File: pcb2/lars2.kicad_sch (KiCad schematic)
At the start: 32 parts, among them SW1 RotaryEncoder_Switch, SW2 SW_Push, SW3 SW_Push, SW4 SW_Push, SW5 SW_Push, SW6 SW_Push, SW7 SW_Push, SW8 SW_Push, SW9 SW_Push, U1 Pico, U2 Charger, U3 MOSFET, U4 MOSFET, U5 MOSFET, U6 STEP_UP, U7 STEP_UP, U8 STEP_UP

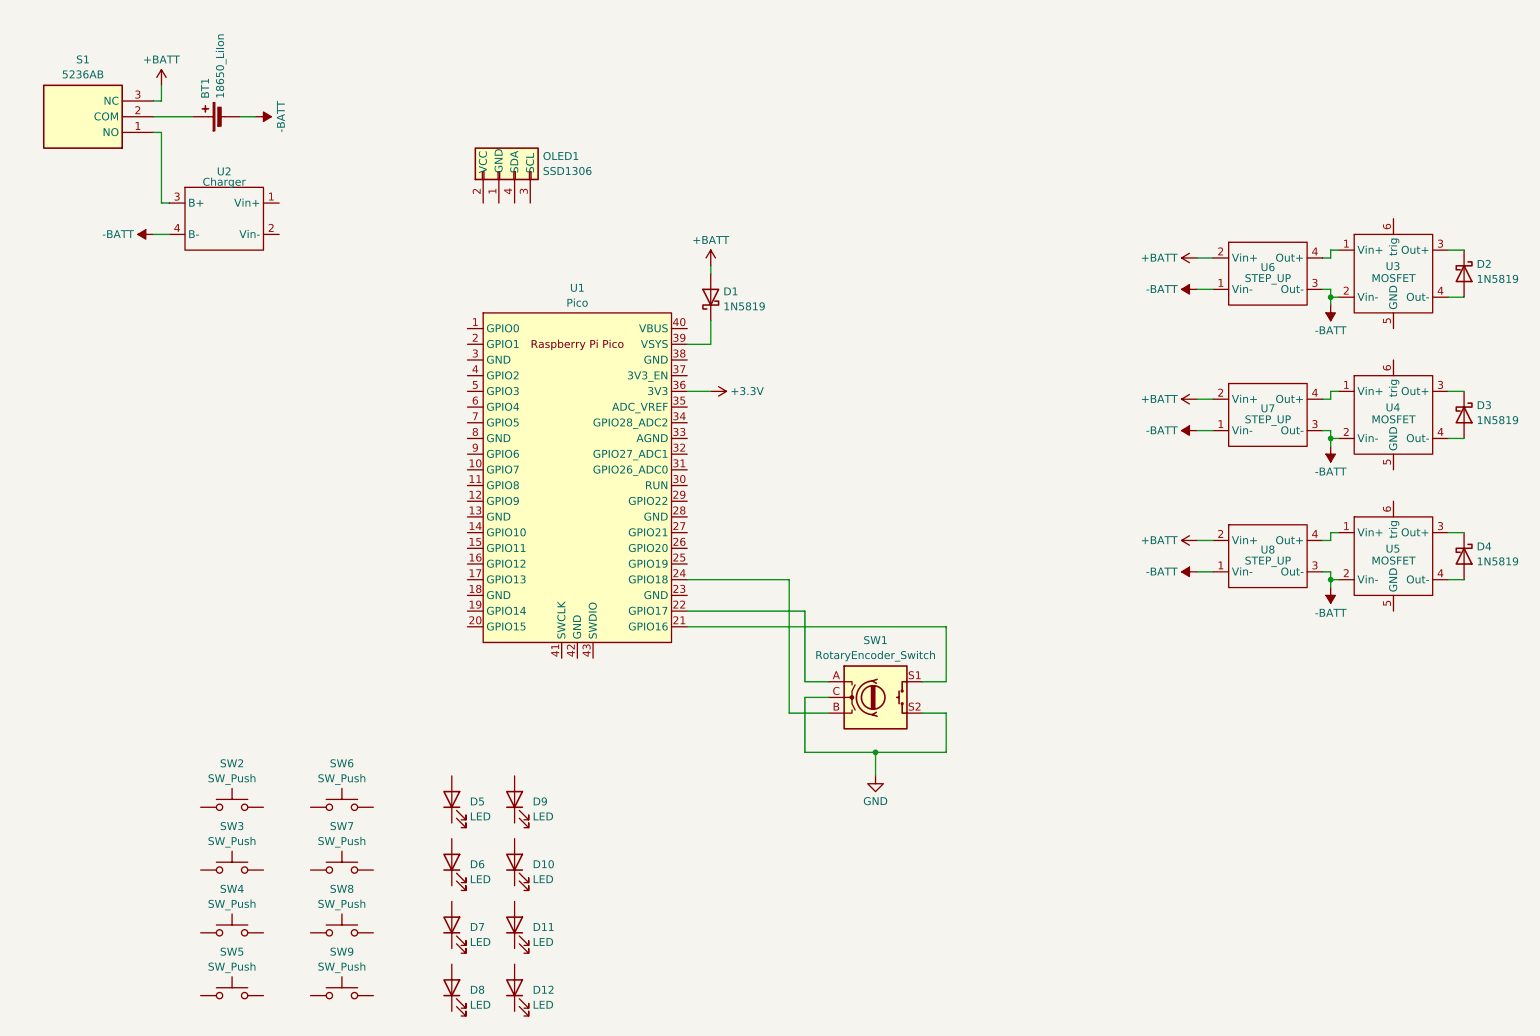
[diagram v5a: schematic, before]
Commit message: add batt- plane
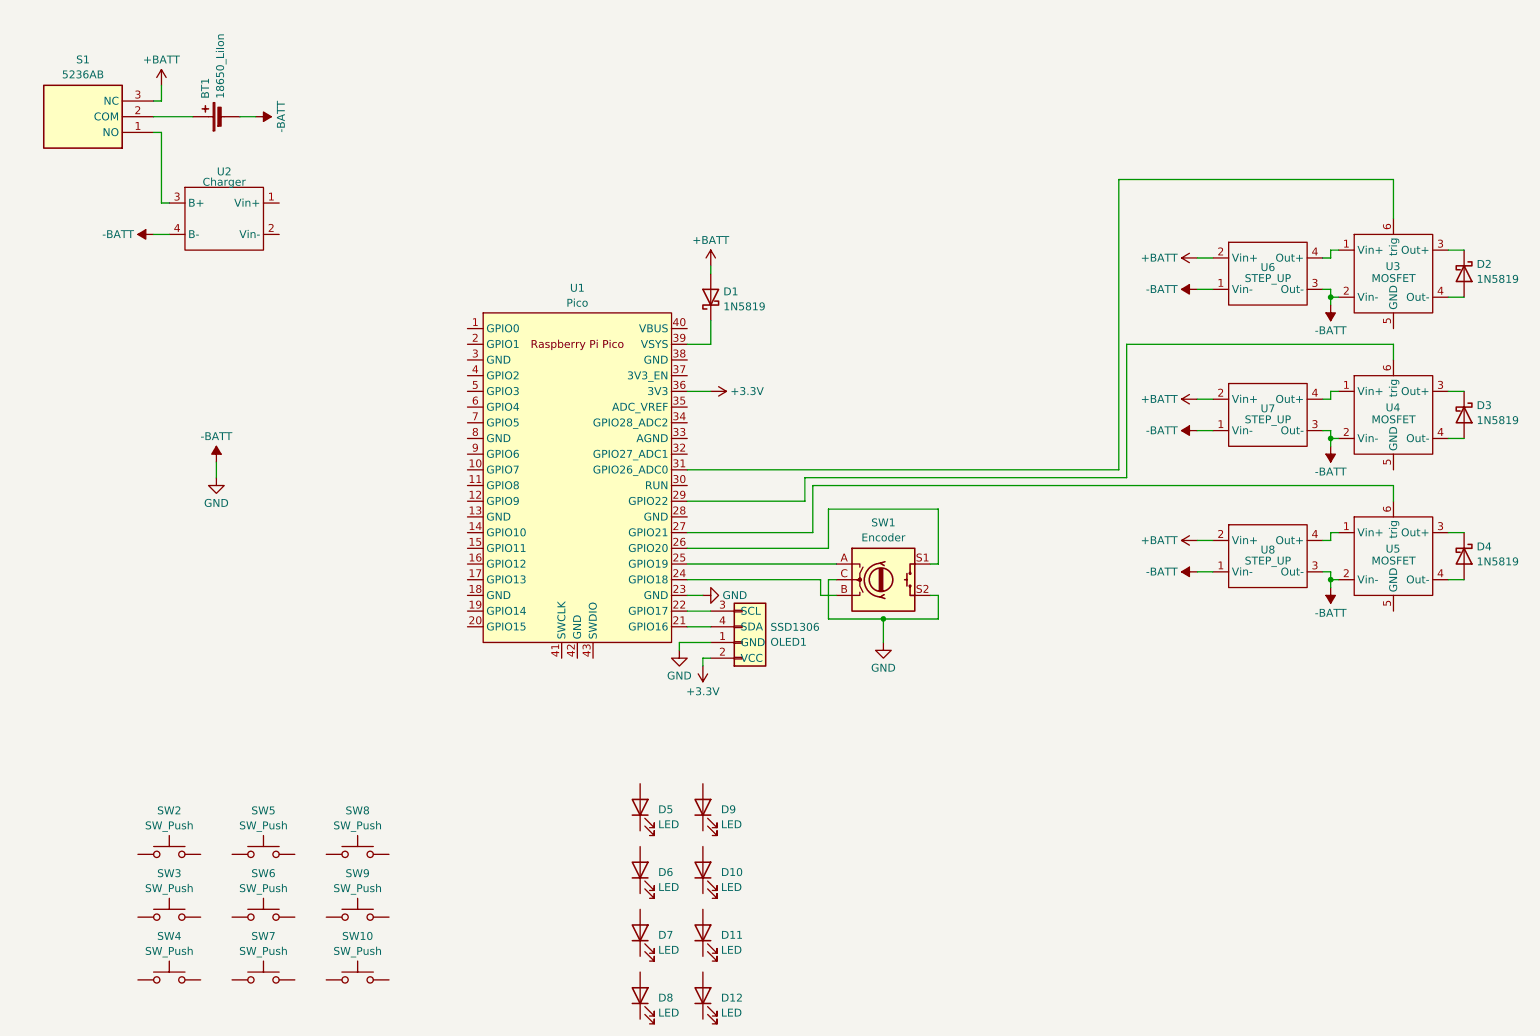
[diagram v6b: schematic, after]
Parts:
- added SW10: SW_Push, Button_Switch_THT:SW_PUSH_6mm_H5mm, symbol Switch:SW_Push
- SW1: value RotaryEncoder_Switch -> Encoder
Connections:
- net GND is gone; now on net -BATT: SW1.C, SW1.S2
- net +3.3V: now also OLED1.2 (VCC)
- net -BATT: now also OLED1.1 (GND), U1.23 (GND)
- net at U3.6 (trig): now also U1.31 (GPIO26_ADC0)
- net at OLED1.3 (SCL): now also U1.22 (GPIO17)
- net at OLED1.4 (SDA): now also U1.21 (GPIO16)
- net at U4.6 (trig): now also U1.29 (GPIO22)
- net at SW1.S1: now also U1.26 (GPIO20); no longer U1.21 (GPIO16)
- net at SW1.A: now also U1.25 (GPIO19); no longer U1.22 (GPIO17)
- net at U1.27 (GPIO21): now also U5.6 (trig)
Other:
- moved on the sheet: D10, D11, D12, D5, D6, D7, D8, D9, OLED1, SW1, SW2, SW3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

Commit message: add battery voltage divider to pcb2
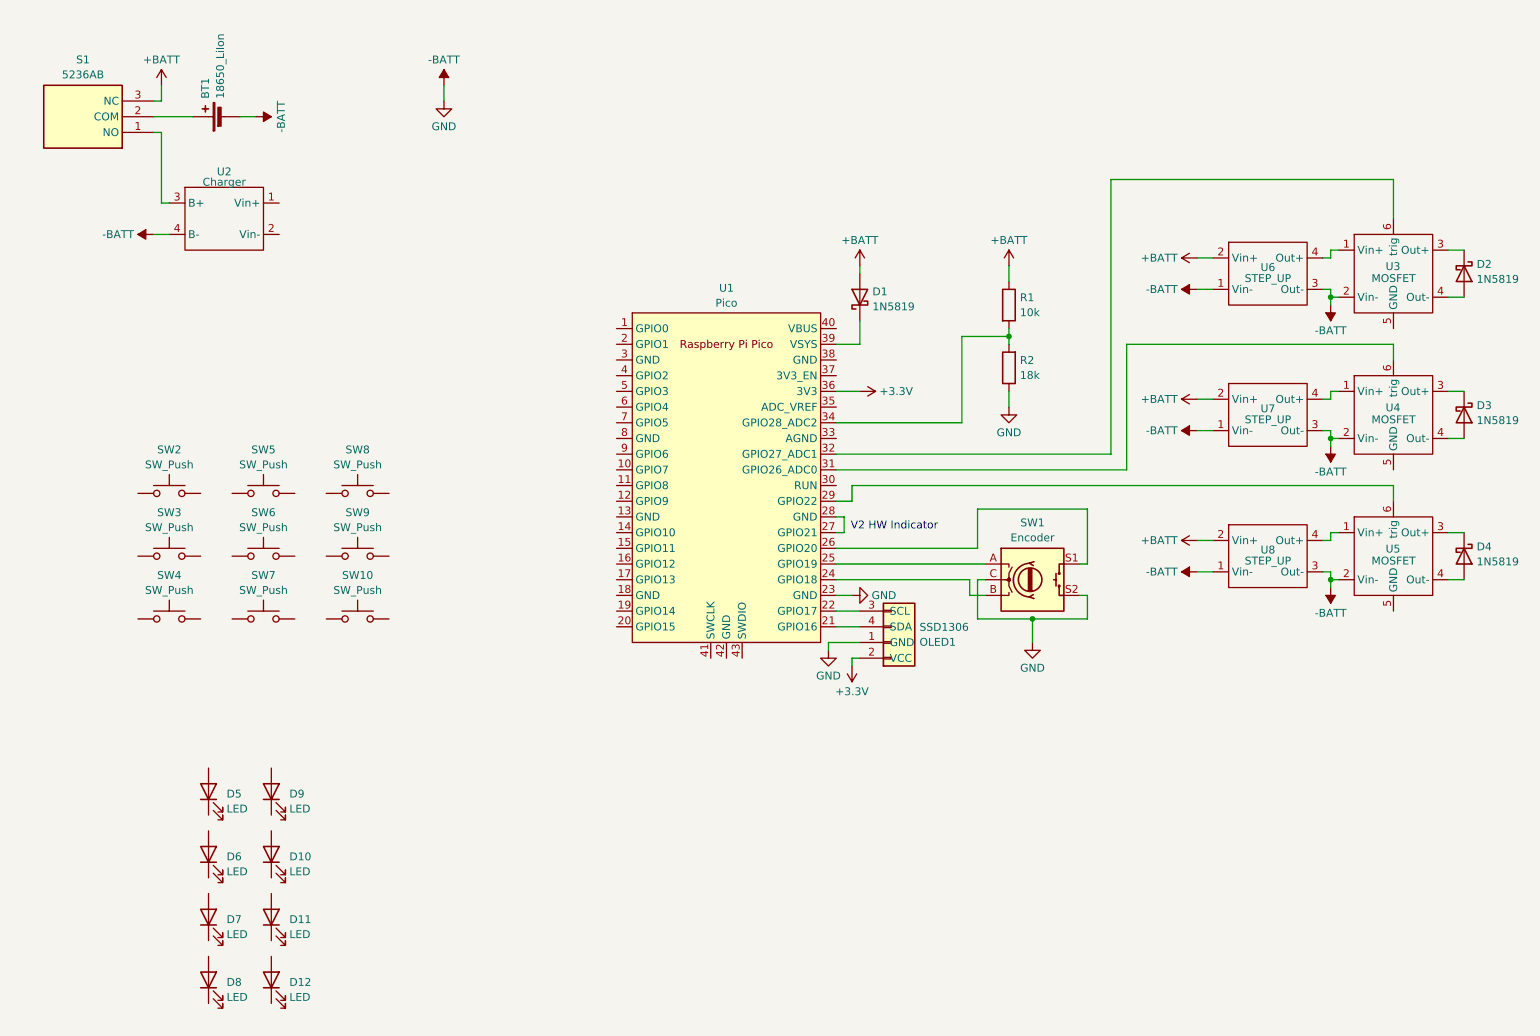
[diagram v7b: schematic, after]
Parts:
- added R1: 10k, Resistor_THT:R_Axial_DIN0204_L3.6mm_D1.6mm_P2.54mm_Vertical, symbol Device:R
- added R2: 18k, Resistor_THT:R_Axial_DIN0204_L3.6mm_D1.6mm_P2.54mm_Vertical, symbol Device:R
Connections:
- net +BATT: now also R1.1
- net -BATT: now also R2.1
- net at U3.6 (trig): now also U1.32 (GPIO27_ADC1); no longer U1.31 (GPIO26_ADC0)
- net at U4.6 (trig): now also U1.31 (GPIO26_ADC0); no longer U1.29 (GPIO22)
- net at U1.27 (GPIO21): now also U1.28 (GND); no longer U5.6 (trig)
- net at U1.34 (GPIO28_ADC2): now also R1.2, R2.2
- new net: U1.29 (GPIO22), U5.6 (trig)
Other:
- note added: "V2 HW Indicator"
- moved on the sheet: D1, D10, D11, D12, D5, D6, D7, D8, D9, OLED1, SW1, SW10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

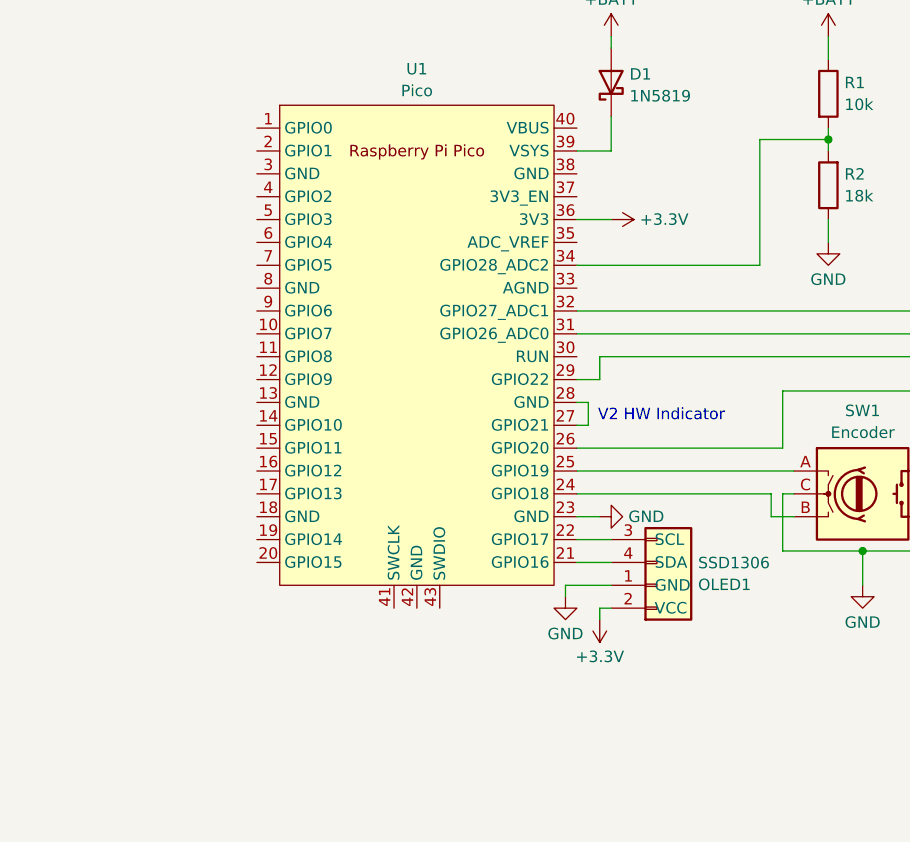
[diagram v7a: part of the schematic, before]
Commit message: add second ground plane
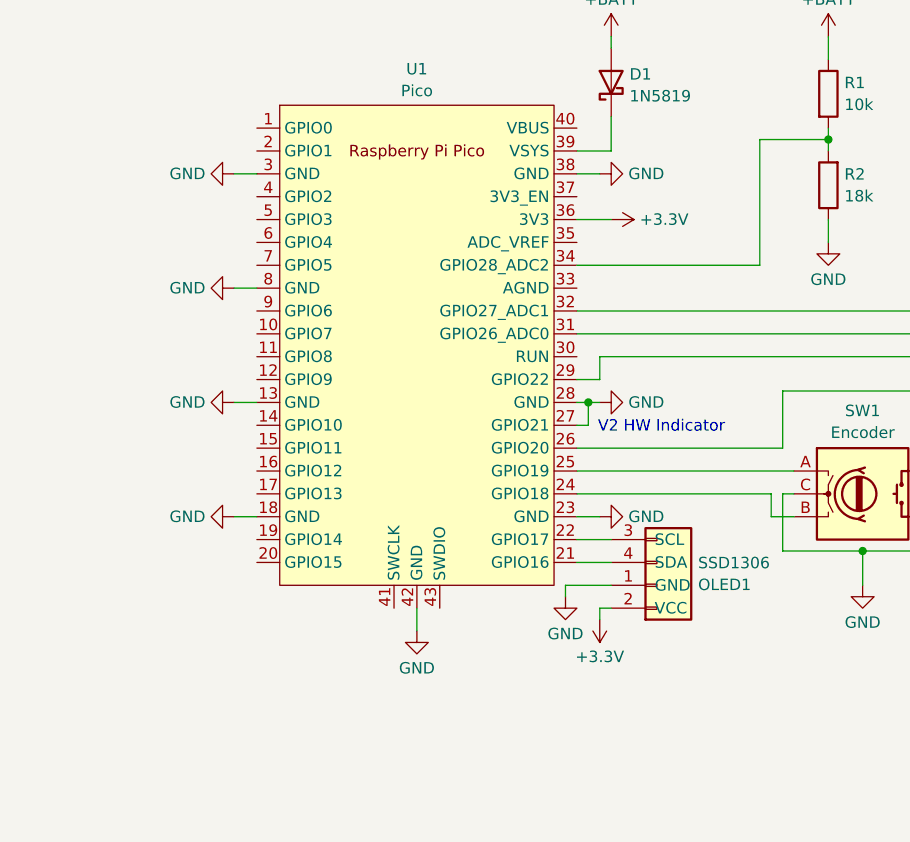
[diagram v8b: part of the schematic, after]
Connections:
- net -BATT: now also U1.13 (GND), U1.18 (GND), U1.27 (GPIO21), U1.28 (GND), U1.3 (GND), U1.38 (GND), U1.42 (GND), U1.8 (GND)
